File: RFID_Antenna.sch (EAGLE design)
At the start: 17 parts, among them J1 U.FL

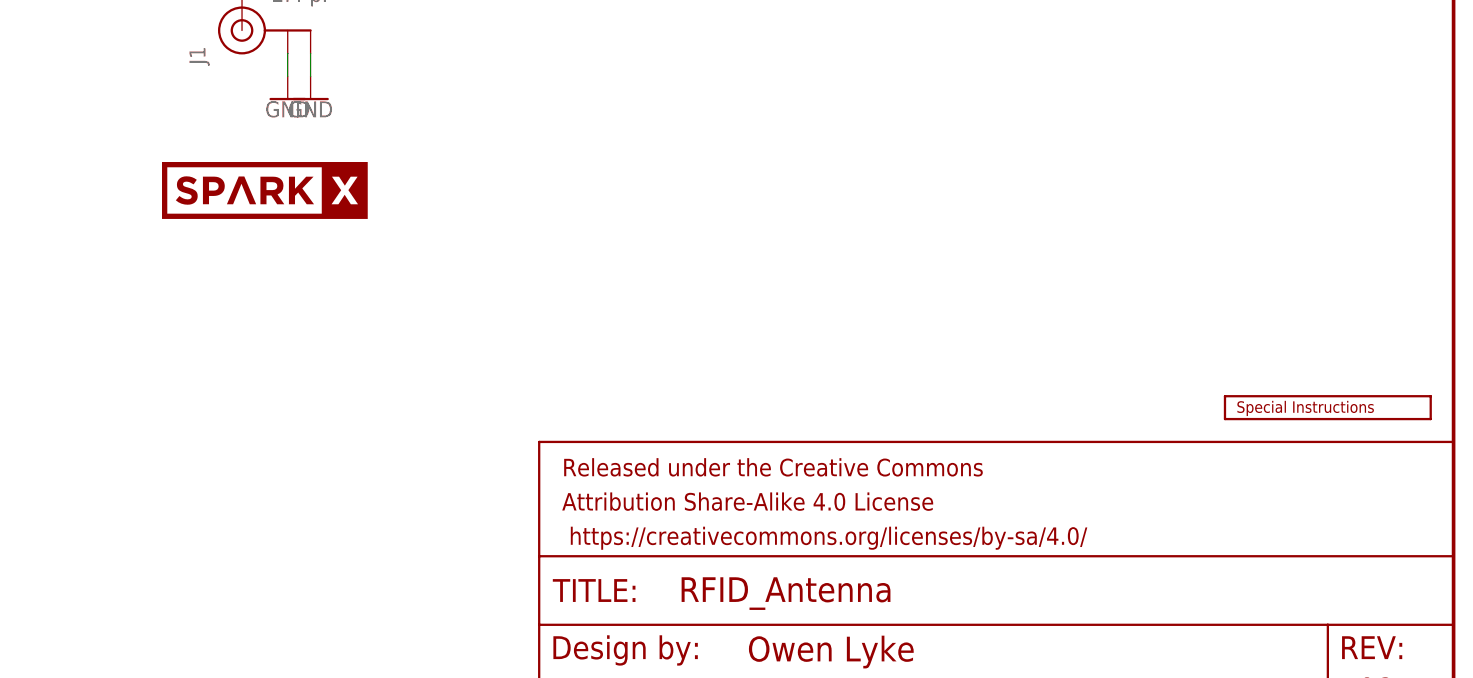
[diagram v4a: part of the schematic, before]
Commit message: Linked SparkX logo between schematic and brd
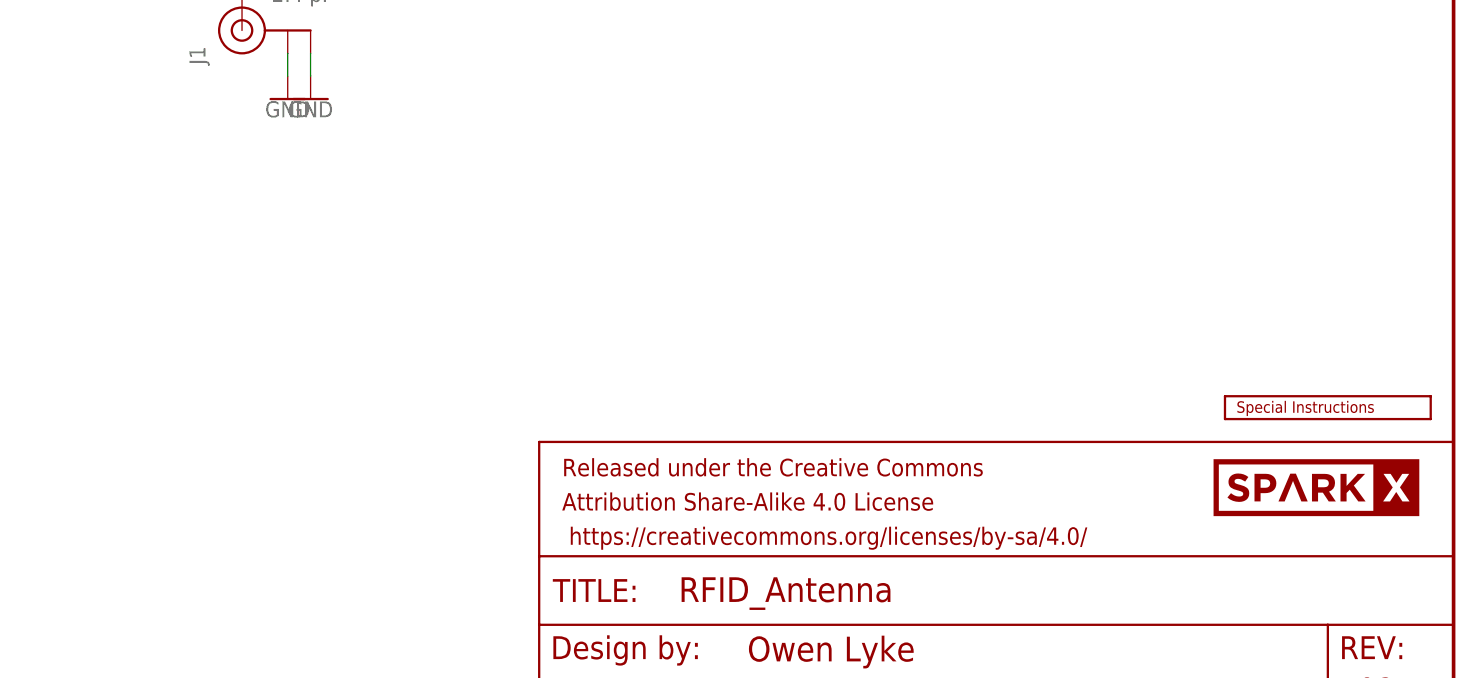
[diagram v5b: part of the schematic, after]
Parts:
- U$12: value SPARKX-LOGO6 -> SPARKX-LOGO5; device SparkX:SPARKX-LOGO6 -> SparkX:SPARKX-LOGO5
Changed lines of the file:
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@@
 <part name="U$1" library="special_parts" deviceset="ANTENNA" device=""/>
 <part name="U$2" library="SparkFun-Aesthetics" deviceset="SPECIAL_INSTRUCTIONS" device="-ORDERING"/>
-<part name="U$12" library="SparkX" deviceset="SPARKX-LOGO" device="6"/>
+<part name="U$12" library="SparkX" deviceset="SPARKX-LOGO" device="5" value="SPARKX-LOGO5"/>
 </parts>
 <sheets>
@@
 <instance part="U$1" gate="G$1" x="114.3" y="137.16" smashed="yes"/>
 <instance part="U$2" gate="G$1" x="223.52" y="38.1" smashed="yes"/>
-<instance part="U$12" gate="G$1" x="116.84" y="63.5" smashed="yes"/>
+<instance part="U$12" gate="G$1" x="233.68" y="30.48" smashed="yes"/>
 </instances>
 <busses>
